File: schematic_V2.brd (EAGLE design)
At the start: 77.7 x 62.1 mm, 20 parts, among them IC1 LD117AS33TR, J1 POWER_JACKPTH

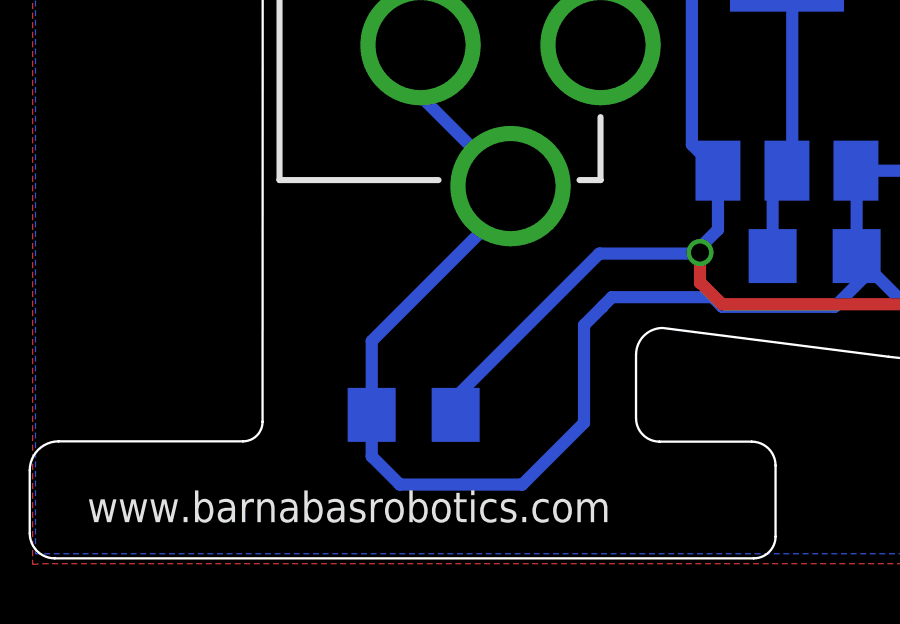
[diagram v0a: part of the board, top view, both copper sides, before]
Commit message: Vincent added mounting holes
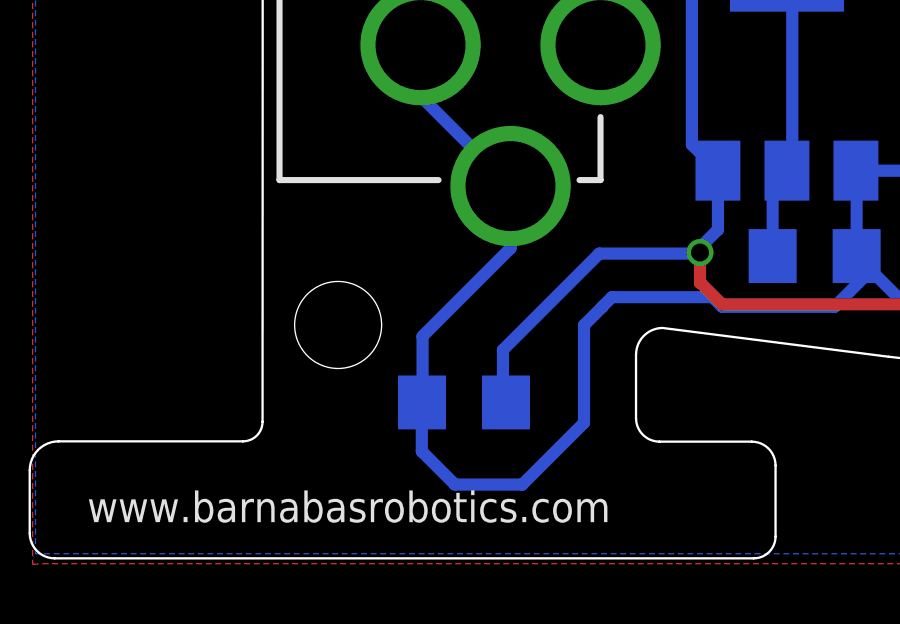
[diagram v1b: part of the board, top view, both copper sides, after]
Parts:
- moved C1 1.73 mm to (14.6, 5.26)
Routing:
- net GND: track 244.4 -> 241.9 mm
- net VIN: track 78.7 -> 77.7 mm
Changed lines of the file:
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@@
 <text x="66.954" y="33.307" size="1.27" layer="21" font="vector" ratio="15" rot="R90">SERVO3</text>
 <text x="59.081" y="33.487" size="1.27" layer="21" font="vector" ratio="15" rot="R90">SERVO4</text>
+<hole x="10.41949375" y="7.83880625" drill="2.9"/>
 </plain>
 <attributes>
@@
 <attribute name="NAME" x="30.103084375" y="21.219159375" size="1.27" layer="25" font="vector" ratio="15" rot="R180"/>
 </element>
-<element name="C1" library="adafruit" package="C1206" value="" x="12.93768125" y="4.8422875" smashed="yes" rot="MR0">
-<attribute name="NAME" x="13.91255" y="5.995996875" size="1.27" layer="26" font="vector" ratio="18" rot="MR0"/>
-<attribute name="VALUE" x="15.47768125" y="1.0322875" size="1.27" layer="28" ratio="10" rot="MR0"/>
+<element name="C1" library="adafruit" package="C1206" value="" x="14.61568125" y="5.2562875" smashed="yes" rot="MR0">
+<attribute name="NAME" x="15.59055" y="6.409996875" size="1.27" layer="26" font="vector" ratio="18" rot="MR0"/>
+<attribute name="VALUE" x="17.15568125" y="1.4462875" size="1.27" layer="28" ratio="10" rot="MR0"/>
 </element>
 <element name="IC1" library="v-reg" package="SOT223" value="LD117AS33TR" x="25.38074375" y="16.132028125" smashed="yes" rot="MR0"/>
@@
 <wire x1="39.523" y1="11.223821875" x2="39.523" y2="10.25" width="0.4064" layer="16"/>
 <wire x1="39.523" y1="10.25" x2="39.438" y2="10.165" width="0.4064" layer="16"/>
-<wire x1="11.53768125" y1="4.8422875" x2="11.53768125" y2="3.458953125" width="0.4064" layer="16"/>
-<wire x1="11.53768125" y1="3.458953125" x2="12.477484375" y2="2.51915" width="0.4064" layer="16"/>
-<wire x1="12.477484375" y1="2.51915" x2="16.557796875" y2="2.51915" width="0.4064" layer="16"/>
 <wire x1="16.557796875" y1="2.51915" x2="18.615696875" y2="4.57705" width="0.4064" layer="16"/>
 <wire x1="18.615696875" y1="4.57705" x2="18.615696875" y2="7.829471875" width="0.4064" layer="16"/>
 <wire x1="18.615696875" y1="7.829471875" x2="19.230703125" y2="8.444478125" width="0.4064" layer="16"/>
 <wire x1="26.96508125" y1="8.444" x2="28.18003125" y2="9.65895" width="0.4064" layer="16"/>
-<wire x1="16.1662125" y1="12.468290625" x2="16.1662125" y2="11.9302125" width="0.4064" layer="16"/>
-<wire x1="16.1662125" y1="11.9302125" x2="11.539" y2="7.303" width="0.4064" layer="16"/>
-<wire x1="11.539" y1="7.303" x2="11.539" y2="4.84360625" width="0.4064" layer="16"/>
-<wire x1="11.539" y1="4.84360625" x2="11.53768125" y2="4.8422875" width="0.4064" layer="16"/>
 <wire x1="19.230703125" y1="8.444478125" x2="19.230703125" y2="8.450703125" width="0.4064" layer="16"/>
 <wire x1="19.230703125" y1="8.450703125" x2="19.546" y2="8.766" width="0.4064" layer="16"/>
@@
 <wire x1="62.441" y1="52.247" x2="62.441" y2="47.308928125" width="0.4064" layer="1"/>
 <wire x1="62.441" y1="47.308928125" x2="61.15846875" y2="46.026396875" width="0.4064" layer="1"/>
+<wire x1="16.557796875" y1="2.51915" x2="14.31285" y2="2.51915" width="0.4064" layer="16"/>
+<wire x1="14.31285" y1="2.51915" x2="13.208" y2="3.624" width="0.4064" layer="16"/>
+<wire x1="13.208" y1="3.624" x2="13.208" y2="5.24860625" width="0.4064" layer="16"/>
+<wire x1="13.208" y1="5.24860625" x2="13.21568125" y2="5.2562875" width="0.4064" layer="16"/>
+<wire x1="16.1662125" y1="12.468290625" x2="16.1662125" y2="10.3952125" width="0.4064" layer="16"/>
+<wire x1="16.1662125" y1="10.3952125" x2="13.234" y2="7.463" width="0.4064" layer="16"/>
+<wire x1="13.234" y1="7.463" x2="13.234" y2="5.27460625" width="0.4064" layer="16"/>
+<wire x1="13.234" y1="5.27460625" x2="13.21568125" y2="5.2562875" width="0.4064" layer="16"/>
 </signal>
 <signal name="AREF">
@@
 <wire x1="22.50678125" y1="9.236884375" x2="23.2164" y2="8.527265625" width="0.4064" layer="1"/>
 <wire x1="22.4713" y1="10.24218125" x2="22.483128125" y2="10.254009375" width="0.4064" layer="16"/>
-<wire x1="14.33768125" y1="4.8422875" x2="14.33768125" y2="5.43195" width="0.4064" layer="16"/>
-<wire x1="14.33768125" y1="5.43195" x2="19.124259375" y2="10.218528125" width="0.4064" layer="16"/>
 <wire x1="19.124259375" y1="10.218528125" x2="22.447646875" y2="10.218528125" width="0.4064" layer="16"/>
 <wire x1="22.447646875" y1="10.218528125" x2="22.483128125" y2="10.254009375" width="0.4064" layer="16"/>
+<wire x1="16.01568125" y1="5.2562875" x2="15.9827125" y2="5.2562875" width="0.4064" layer="16"/>
+<wire x1="15.9827125" y1="5.2562875" x2="15.913" y2="5.326" width="0.4064" layer="16"/>
+<wire x1="15.913" y1="5.326" x2="15.913" y2="7.00726875" width="0.4064" layer="16"/>
+<wire x1="15.913" y1="7.00726875" x2="19.124259375" y2="10.218528125" width="0.4064" layer="16"/>
 </signal>
 <signal name="+5V">

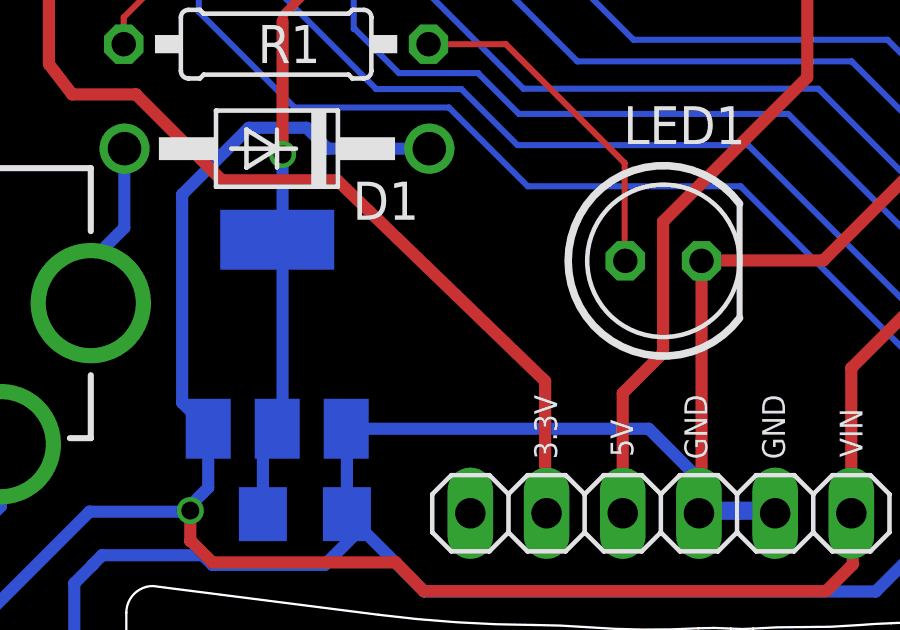
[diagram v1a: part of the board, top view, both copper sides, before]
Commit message: Add files via upload
5VS and +5V rails merged
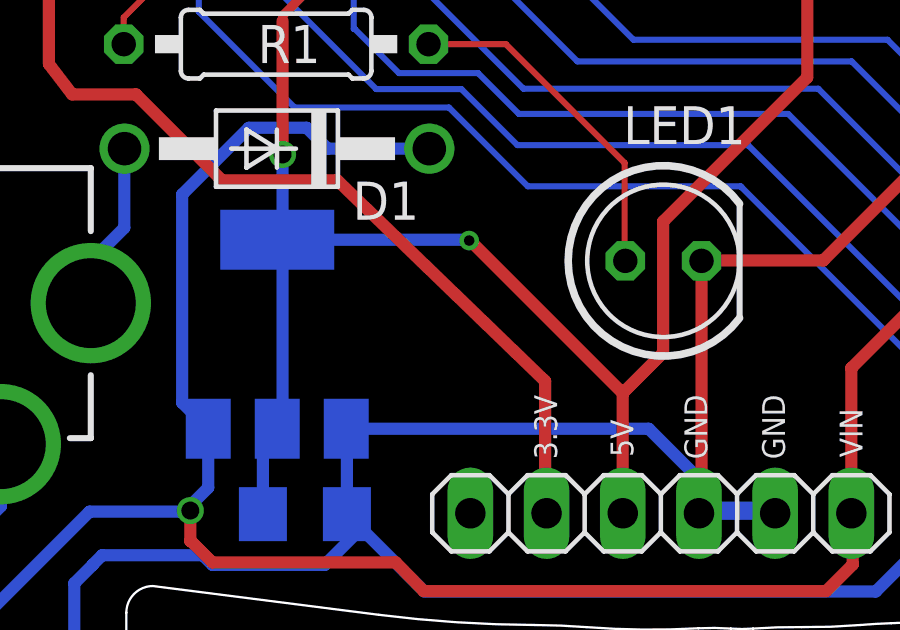
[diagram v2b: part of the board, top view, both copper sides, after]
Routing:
- net +5V: track 21.5 -> 28.7 mm
- net 5VS: track 115.4 -> 122.0 mm
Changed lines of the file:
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@@
 <?xml version="1.0" encoding="utf-8"?>
 <!DOCTYPE eagle SYSTEM "eagle.dtd">
-<eagle version="7.5.0">
+<eagle version="9.0.1">
 <drawing>
 <settings>
 <setting alwaysvectorfont="no"/>
+<setting keepoldvectorfont="yes"/>
 <setting verticaltext="up"/>
 </settings>
@@
 <param name="dpMaxLengthDifference" value="10mm"/>
 <param name="dpGapFactor" value="2.5"/>
-<param name="checkGrid" value="0"/>
 <param name="checkAngle" value="0"/>
 <param name="checkFont" value="1"/>
 <param name="checkRestrict" value="0"/>
+<param name="checkStop" value="0"/>
+<param name="checkValues" value="0"/>
 <param name="useDiameter" value="13"/>
 <param name="maxErrors" value="50"/>
@@
 <element name="BUZZER" library="buzzer" package="F/TMB" value="F/TMB" x="62.073796875" y="20.80250625" smashed="yes">
 <attribute name="MF" value="" x="62.073796875" y="20.80250625" size="1.778" layer="27" display="off"/>
-<attribute name="OC_NEWARK" value="unknown" x="62.073796875" y="20.80250625" size="1.778" layer="27" display="off"/>
-<attribute name="OC_FARNELL" value="unknown" x="62.073796875" y="20.80250625" size="1.778" layer="27" display="off"/>
 <attribute name="MPN" value="" x="62.073796875" y="20.80250625" size="1.778" layer="27" display="off"/>
 <attribute name="NAME" x="63.459825" y="13.401359375" size="0.8128" layer="25" font="vector" ratio="15"/>
+<attribute name="OC_FARNELL" value="unknown" x="62.073796875" y="20.80250625" size="1.778" layer="27" display="off"/>
+<attribute name="OC_NEWARK" value="unknown" x="62.073796875" y="20.80250625" size="1.778" layer="27" display="off"/>
 </element>
 <element name="J1" library="SparkFun" package="POWER_JACK_PTH" value="POWER_JACKPTH" x="5.4662125" y="17.168290625" smashed="yes" rot="R270"/>
@@
 <wire x1="43.047" y1="24.692" x2="43.047" y2="28.9478" width="0.4064" layer="1"/>
 <wire x1="43.047" y1="28.9478" x2="43.1704" y2="29.0712" width="0.4064" layer="1"/>
+<wire x1="36.898" y1="14.168" x2="31.881" y2="19.185" width="0.4064" layer="1"/>
+<wire x1="31.881" y1="19.185" x2="31.824" y2="19.185" width="0.4064" layer="1"/>
 </signal>
 <signal name="3V3">
@@
 <wire x1="26.647" y1="27.838" x2="26.647" y2="32.42" width="0.3048" layer="1"/>
 <wire x1="26.647" y1="32.42" x2="26.634" y2="32.433" width="0.3048" layer="1"/>
+<wire x1="25.38074375" y1="19.282028125" x2="31.843971875" y2="19.282028125" width="0.4064" layer="16"/>
+<wire x1="31.843971875" y1="19.282028125" x2="31.894" y2="19.232" width="0.4064" layer="16"/>
+</signal>
+<signal name="N$3">
+<via x="31.778" y="19.255" extent="1-16" drill="0.35"/>
 </signal>
 </signals>
-<errors>
-</errors>
 </board>
 </drawing>
